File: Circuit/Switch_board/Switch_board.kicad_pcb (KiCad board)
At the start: 2 copper layers, 50.8 x 31.7 mm, 31 parts, among them J1 switch_mode, J2 switch, P1 XT30, Q1 2N7002, Q2 2N7002, Q3 2N7002, Q4 2N7002, U1 DRV5023

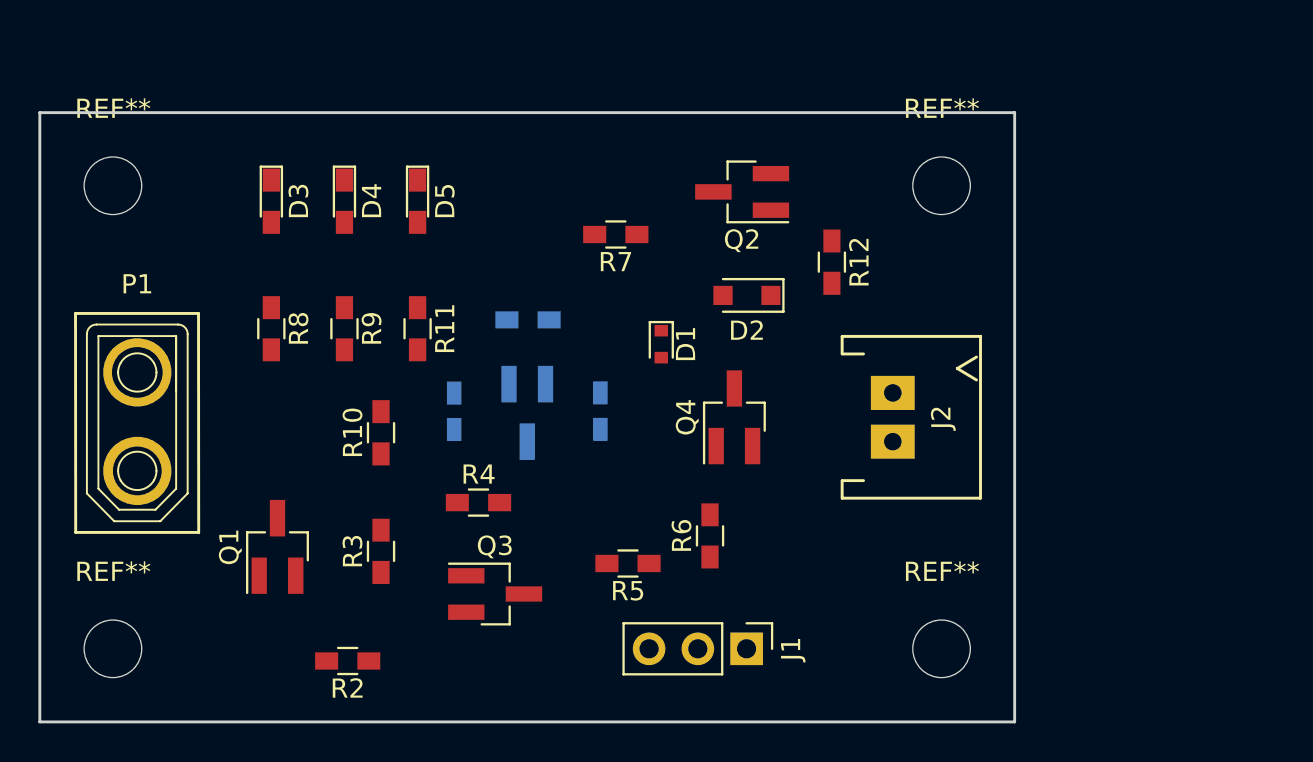
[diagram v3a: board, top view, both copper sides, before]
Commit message: added traces into pcb of Switch_board
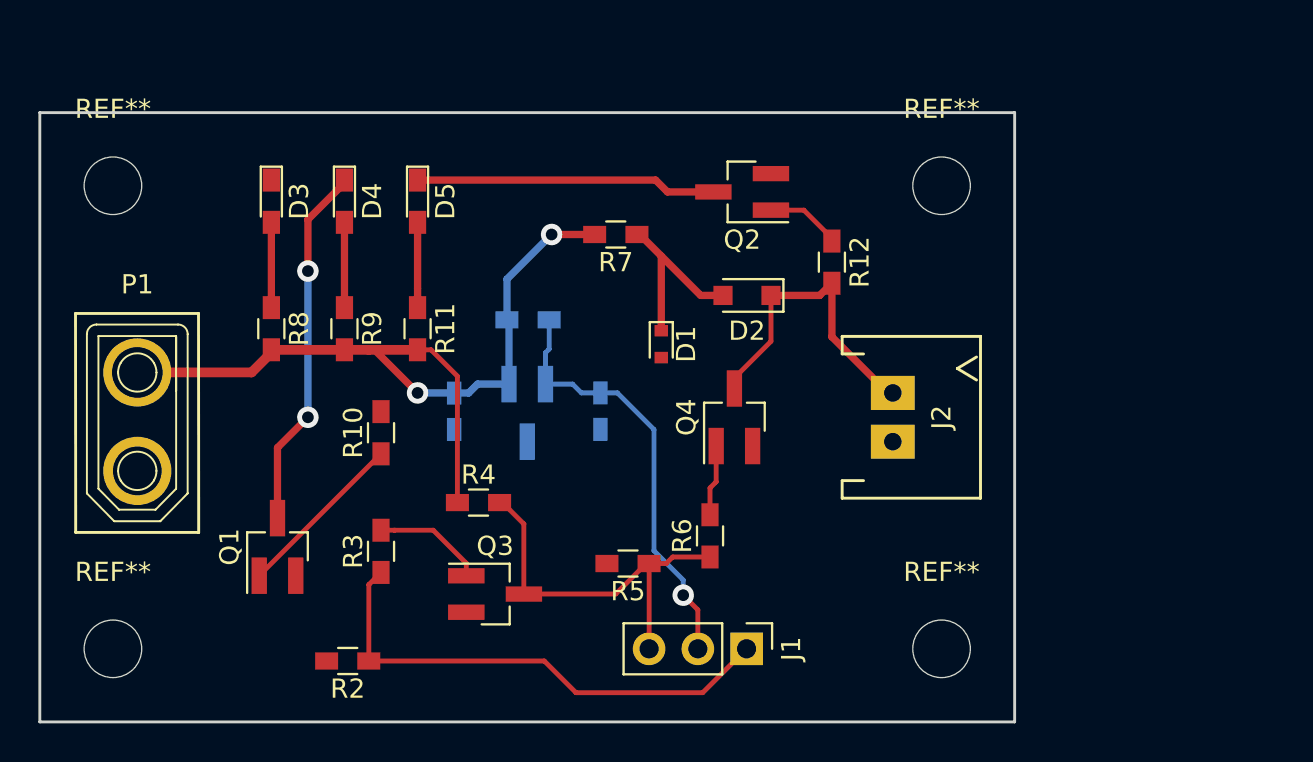
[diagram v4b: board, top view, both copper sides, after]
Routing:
- net VCC: track 0.00 -> 43.9 mm, vias 0 -> 2
- net Net-(J1-Pad1): track 0.00 -> 26.2 mm
- net hall_sensor_out: track 0.00 -> 22.4 mm, vias 0 -> 1
- net Net-(J1-Pad3): track 0.00 -> 20.3 mm
- net Net-(D4-Pad1): track 0.00 -> 19.1 mm, vias 0 -> 2
- net +switch: track 0.00 -> 16.3 mm
- net Net-(D5-Pad1): track 0.00 -> 15.7 mm
- net Net-(D1-Pad1): track 0.00 -> 9.70 mm
- net Net-(Q1-Pad1): track 0.00 -> 8.98 mm
- net Net-(Q3-Pad1): track 0.00 -> 5.81 mm
- net Net-(D5-Pad2): track 0.00 -> 4.44 mm
- net Net-(D4-Pad2): track 0.00 -> 4.44 mm
- net Net-(D3-Pad2): track 0.00 -> 4.44 mm
- net Net-(Q2-Pad1): track 0.00 -> 3.93 mm
- net Net-(Q4-Pad1): track 0.00 -> 3.71 mm
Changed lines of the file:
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@@
 (kicad_pcb (version 4) (host pcbnew 4.0.7)
   (general
-    (links 0)
+    (links 44)
     (no_connects 44)
-    (area 135.168857 102.398142 190.979 141.493286)
+    (area 136.041714 103.668142 194.158286 141.019)
     (thickness 1.6)
     (drawings 4)
-    (tracks 0)
+    (tracks 93)
     (zones 0)
     (modules 31)
@@
   (setup
     (last_trace_width 0.254)
+    (user_trace_width 0.381)
+    (user_trace_width 0.508)
     (trace_clearance 0.254)
     (zone_clearance 0.508)
@@
   (gr_line (start 190.5 139.7) (end 190.5 107.95) (layer Edge.Cuts) (width 0.15))
   (gr_line (start 139.7 139.7) (end 190.5 139.7) (layer Edge.Cuts) (width 0.15))
+  (segment (start 161.46 128.27) (end 161.46 121.681) (width 0.254) (layer F.Cu) (net 1))
+  (segment (start 161.46 121.681) (end 160.089 120.31) (width 0.254) (layer F.Cu) (net 1))
+  (segment (start 160.089 120.31) (end 159.385 120.31) (width 0.254) (layer F.Cu) (net 1))
+  (segment (start 166.37 114.3) (end 168.615 114.3) (width 0.381) (layer F.Cu) (net 1))
+  (segment (start 164.043 118.745) (end 164.043 116.627) (width 0.381) (layer B.Cu) (net 1))
+  (segment (start 164.043 116.627) (end 166.37 114.3) (width 0.381) (layer B.Cu) (net 1))
+  (segment (start 164.15 122.095) (end 164.15 118.852) (width 0.381) (layer B.Cu) (net 1))
+  (segment (start 164.15 118.852) (end 164.043 118.745) (width 0.381) (layer B.Cu) (net 1))
+  (segment (start 162.046 122.56) (end 162.511 122.095) (width 0.381) (layer B.Cu) (net 1))
+  (segment (start 162.511 122.095) (end 164.15 122.095) (width 0.381) (layer B.Cu) (net 1))
+  (segment (start 161.29 122.56) (end 162.046 122.56) (width 0.381) (layer B.Cu) (net 1))
+  (segment (start 159.385 122.555) (end 161.285 122.555) (width 0.381) (layer B.Cu) (net 1))
+  (segment (start 161.285 122.555) (end 161.29 122.56) (width 0.381) (layer B.Cu) (net 1))
+  (segment (start 156.845 120.31) (end 157.14 120.31) (width 0.381) (layer F.Cu) (net 1))
+  (segment (start 157.14 120.31) (end 159.385 122.555) (width 0.381) (layer F.Cu) (net 1))
+  (segment (start 156.845 120.31) (end 159.385 120.31) (width 0.508) (layer F.Cu) (net 1))
+  (segment (start 155.575 120.31) (end 156.845 120.31) (width 0.508) (layer F.Cu) (net 1))
+  (via (at 166.37 114.3) (size 1.1176) (drill 0.6096) (layers F.Cu B.Cu) (net 1))
+  (via (at 159.385 122.555) (size 1.1176) (drill 0.6096) (layers F.Cu B.Cu) (net 1))
+  (segment (start 151.765 120.31) (end 155.575 120.31) (width 0.508) (layer F.Cu) (net 1))
+  (segment (start 144.78 121.4882) (end 150.7368 121.4882) (width 0.508) (layer F.Cu) (net 1))
+  (segment (start 150.7368 121.4882) (end 151.765 120.46) (width 0.508) (layer F.Cu) (net 1))
+  (segment (start 151.765 120.46) (end 151.765 120.31) (width 0.508) (layer F.Cu) (net 1))
+  (segment (start 172.085 115.42) (end 174.14 117.475) (width 0.381) (layer F.Cu) (net 3))
+  (segment (start 174.14 117.475) (end 175.3 117.475) (width 0.381) (layer F.Cu) (net 3))
+  (segment (start 172.085 115.42) (end 172.085 119.315) (width 0.381) (layer F.Cu) (net 3))
+  (segment (start 170.815 114.3) (end 170.965 114.3) (width 0.381) (layer F.Cu) (net 3))
+  (segment (start 170.965 114.3) (end 172.085 115.42) (width 0.381) (layer F.Cu) (net 3))
+  (segment (start 174.244 138.176) (end 176.53 135.89) (width 0.254) (layer F.Cu) (net 4))
+  (segment (start 167.64 138.176) (end 174.244 138.176) (width 0.254) (layer F.Cu) (net 4))
+  (segment (start 165.989 136.525) (end 167.64 138.176) (width 0.254) (layer F.Cu) (net 4))
+  (segment (start 156.845 136.525) (end 165.989 136.525) (width 0.254) (layer F.Cu) (net 4))
+  (segment (start 156.845 136.525) (end 156.845 132.545) (width 0.254) (layer F.Cu) (net 4))
+  (segment (start 156.845 132.545) (end 157.48 131.91) (width 0.254) (layer F.Cu) (net 4))
+  (segment (start 171.45 131.445) (end 171.45 135.89) (width 0.254) (layer F.Cu) (net 5))
+  (segment (start 172.339 131.445) (end 172.679 131.105) (width 0.254) (layer F.Cu) (net 5))
+  (segment (start 172.679 131.105) (end 174.625 131.105) (width 0.254) (layer F.Cu) (net 5))
+  (segment (start 171.45 131.445) (end 172.339 131.445) (width 0.254) (layer F.Cu) (net 5))
+  (segment (start 164.925 133.035) (end 169.71 133.035) (width 0.254) (layer F.Cu) (net 5))
+  (segment (start 169.71 133.035) (end 171.3 131.445) (width 0.254) (layer F.Cu) (net 5))
+  (segment (start 171.3 131.445) (end 171.45 131.445) (width 0.254) (layer F.Cu) (net 5))
+  (segment (start 163.66 128.27) (end 163.81 128.27) (width 0.254) (layer F.Cu) (net 5))
+  (segment (start 163.81 128.27) (end 164.925 129.385) (width 0.254) (layer F.Cu) (net 5))
+  (segment (start 164.925 129.385) (end 164.925 133.035) (width 0.254) (layer F.Cu) (net 5))
+  (segment (start 151.135 132.08) (end 151.135 132.075) (width 0.254) (layer F.Cu) (net 6))
+  (segment (start 151.135 132.075) (end 157.48 125.73) (width 0.254) (layer F.Cu) (net 6))
+  (segment (start 177.8 113.03) (end 179.515 113.03) (width 0.254) (layer F.Cu) (net 7))
+  (segment (start 179.515 113.03) (end 180.975 114.49) (width 0.254) (layer F.Cu) (net 7))
+  (segment (start 180.975 114.49) (end 180.975 114.64) (width 0.254) (layer F.Cu) (net 7))
+  (segment (start 166.05 120.462) (end 166.243 120.269) (width 0.254) (layer B.Cu) (net 8))
+  (segment (start 166.243 120.269) (end 166.243 118.745) (width 0.254) (layer B.Cu) (net 8))
+  (segment (start 166.05 122.095) (end 166.05 120.462) (width 0.254) (layer B.Cu) (net 8))
+  (segment (start 167.465 122.095) (end 167.925 122.555) (width 0.254) (layer B.Cu) (net 8))
+  (segment (start 167.925 122.555) (end 168.91 122.555) (width 0.254) (layer B.Cu) (net 8))
+  (segment (start 166.05 122.095) (end 167.465 122.095) (width 0.254) (layer B.Cu) (net 8))
+  (segment (start 173.228 133.096) (end 173.228 132.305738) (width 0.254) (layer B.Cu) (net 8))
+  (segment (start 173.228 132.305738) (end 171.704 130.781738) (width 0.254) (layer B.Cu) (net 8))
+  (segment (start 171.704 130.781738) (end 171.704 124.46) (width 0.254) (layer B.Cu) (net 8))
+  (segment (start 171.704 124.46) (end 169.799 122.555) (width 0.254) (layer B.Cu) (net 8))
+  (segment (start 169.799 122.555) (end 168.91 122.555) (width 0.254) (layer B.Cu) (net 8))
+  (segment (start 173.99 135.89) (end 173.99 133.858) (width 0.254) (layer F.Cu) (net 8))
+  (segment (start 173.99 133.858) (end 173.228 133.096) (width 0.254) (layer F.Cu) (net 8))
+  (via (at 173.228 133.096) (size 1.1176) (drill 0.6096) (layers F.Cu B.Cu) (net 8))
+  (segment (start 175.895 122.325) (end 175.895 121.775) (width 0.254) (layer F.Cu) (net 9))
+  (segment (start 175.895 121.775) (end 177.8 119.87) (width 0.254) (layer F.Cu) (net 9))
+  (segment (start 177.8 119.87) (end 177.8 117.475) (width 0.254) (layer F.Cu) (net 9))
+  (segment (start 180.975 116.84) (end 180.975 119.634) (width 0.381) (layer F.Cu) (net 9))
+  (segment (start 180.975 119.634) (end 183.896 122.555) (width 0.381) (layer F.Cu) (net 9))
+  (segment (start 183.896 122.555) (end 184.15 122.555) (width 0.381) (layer F.Cu) (net 9))
+  (segment (start 177.8 117.475) (end 180.34 117.475) (width 0.381) (layer F.Cu) (net 9))
+  (segment (start 180.34 117.475) (end 180.975 116.84) (width 0.381) (layer F.Cu) (net 9))
+  (segment (start 151.765 118.11) (end 151.765 113.665) (width 0.381) (layer F.Cu) (net 10))
+  (segment (start 153.67 123.825) (end 152.085 125.41) (width 0.381) (layer F.Cu) (net 11))
+  (segment (start 152.085 125.41) (end 152.085 129.08) (width 0.381) (layer F.Cu) (net 11))
+  (segment (start 153.67 116.205) (end 153.67 123.825) (width 0.381) (layer B.Cu) (net 11))
+  (via (at 153.67 123.825) (size 1.1176) (drill 0.6096) (layers F.Cu B.Cu) (net 11))
+  (segment (start 155.575 111.465) (end 155.575 111.615) (width 0.381) (layer F.Cu) (net 11))
+  (segment (start 155.575 111.615) (end 153.67 113.52) (width 0.381) (layer F.Cu) (net 11))
+  (segment (start 153.67 113.52) (end 153.67 116.205) (width 0.381) (layer F.Cu) (net 11))
+  (via (at 153.67 116.205) (size 1.1176) (drill 0.6096) (layers F.Cu B.Cu) (net 11))
+  (segment (start 155.575 118.11) (end 155.575 113.665) (width 0.381) (layer F.Cu) (net 12))
+  (segment (start 171.79 111.465) (end 172.405 112.08) (width 0.381) (layer F.Cu) (net 13))
+  (segment (start 172.405 112.08) (end 174.8 112.08) (width 0.381) (layer F.Cu) (net 13))
+  (segment (start 159.385 111.465) (end 171.79 111.465) (width 0.381) (layer F.Cu) (net 13))
+  (segment (start 159.385 118.11) (end 159.385 117.129) (width 0.381) (layer F.Cu) (net 14))
+  (segment (start 159.385 117.129) (end 159.385 113.665) (width 0.381) (layer F.Cu) (net 14))
+  (segment (start 161.925 132.085) (end 161.925 131.431) (width 0.254) (layer F.Cu) (net 15))
+  (segment (start 161.925 131.431) (end 160.204 129.71) (width 0.254) (layer F.Cu) (net 15))
+  (segment (start 160.204 129.71) (end 158.184 129.71) (width 0.254) (layer F.Cu) (net 15))
+  (segment (start 158.184 129.71) (end 157.48 129.71) (width 0.254) (layer F.Cu) (net 15))
+  (segment (start 174.625 127.508) (end 174.945 127.188) (width 0.254) (layer F.Cu) (net 16))
+  (segment (start 174.945 127.188) (end 174.945 125.325) (width 0.254) (layer F.Cu) (net 16))
+  (segment (start 174.625 128.905) (end 174.625 127.508) (width 0.254) (layer F.Cu) (net 16))
 )

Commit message: filled GND zone for Switch_board
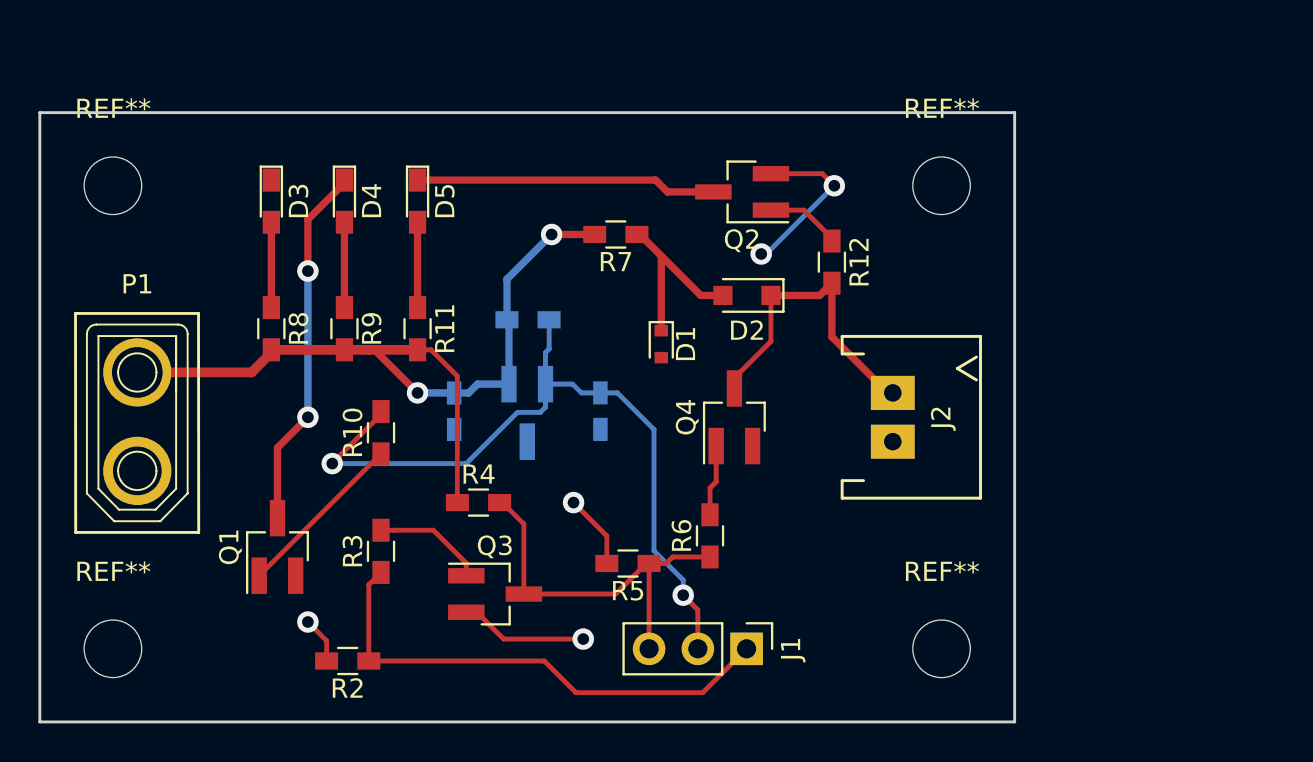
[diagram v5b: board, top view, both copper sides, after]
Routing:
- net GND: track 0.00 -> 21.9 mm, vias 0 -> 5
- net hall_sensor_out: track 22.4 -> 39.7 mm, vias 1 -> 2
- added copper zone on B.Cu, net GND
- added copper zone on F.Cu, net GND
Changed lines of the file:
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@@
   (general
     (links 44)
-    (no_connects 44)
+    (no_connects 0)
     (area 136.041714 103.668142 194.158286 141.019)
     (thickness 1.6)
     (drawings 4)
-    (tracks 93)
+    (tracks 118)
     (zones 0)
     (modules 31)
@@
     (pad_to_mask_clearance 0.2)
     (aux_axis_origin 0 0)
-    (visible_elements FFFFFF7F)
+    (visible_elements FFFFEF7F)
     (pcbplotparams
       (layerselection 0x00030_80000001)
@@
   (segment (start 150.7368 121.4882) (end 151.765 120.46) (width 0.508) (layer F.Cu) (net 1))
   (segment (start 151.765 120.46) (end 151.765 120.31) (width 0.508) (layer F.Cu) (net 1))
+  (segment (start 163.872 135.382) (end 168.021 135.382) (width 0.254) (layer F.Cu) (net 2))
+  (segment (start 161.925 133.985) (end 162.475 133.985) (width 0.254) (layer F.Cu) (net 2))
+  (segment (start 162.475 133.985) (end 163.872 135.382) (width 0.254) (layer F.Cu) (net 2))
+  (segment (start 154.645 136.525) (end 154.645 135.468) (width 0.254) (layer F.Cu) (net 2))
+  (segment (start 154.645 135.468) (end 153.67 134.493) (width 0.254) (layer F.Cu) (net 2))
+  (via (at 153.67 134.493) (size 1.1176) (drill 0.6096) (layers F.Cu B.Cu) (net 2))
+  (via (at 168.021 135.382) (size 1.1176) (drill 0.6096) (layers F.Cu B.Cu) (net 2))
+  (segment (start 181.102 111.76) (end 177.546 115.316) (width 0.254) (layer B.Cu) (net 2))
+  (segment (start 177.546 115.316) (end 177.292 115.316) (width 0.254) (layer B.Cu) (net 2))
+  (via (at 177.292 115.316) (size 1.1176) (drill 0.6096) (layers F.Cu B.Cu) (net 2))
+  (segment (start 177.8 111.13) (end 180.472 111.13) (width 0.254) (layer F.Cu) (net 2))
+  (segment (start 180.472 111.13) (end 181.102 111.76) (width 0.254) (layer F.Cu) (net 2))
+  (via (at 181.102 111.76) (size 1.1176) (drill 0.6096) (layers F.Cu B.Cu) (net 2))
+  (segment (start 169.25 131.445) (end 169.25 130.007) (width 0.254) (layer F.Cu) (net 2))
+  (segment (start 169.25 130.007) (end 167.513 128.27) (width 0.254) (layer F.Cu) (net 2))
+  (via (at 167.513 128.27) (size 1.1176) (drill 0.6096) (layers F.Cu B.Cu) (net 2))
   (segment (start 172.085 115.42) (end 174.14 117.475) (width 0.381) (layer F.Cu) (net 3))
   (segment (start 174.14 117.475) (end 175.3 117.475) (width 0.381) (layer F.Cu) (net 3))
@@
   (segment (start 179.515 113.03) (end 180.975 114.49) (width 0.254) (layer F.Cu) (net 7))
   (segment (start 180.975 114.49) (end 180.975 114.64) (width 0.254) (layer F.Cu) (net 7))
+  (segment (start 154.94 126.238) (end 161.925 126.238) (width 0.254) (layer B.Cu) (net 8))
+  (segment (start 161.925 126.238) (end 164.592 123.571) (width 0.254) (layer B.Cu) (net 8))
+  (segment (start 164.592 123.571) (end 165.778 123.571) (width 0.254) (layer B.Cu) (net 8))
+  (segment (start 165.778 123.571) (end 166.05 123.299) (width 0.254) (layer B.Cu) (net 8))
+  (segment (start 166.05 123.299) (end 166.05 122.095) (width 0.254) (layer B.Cu) (net 8))
+  (segment (start 157.48 123.53) (end 157.48 123.68) (width 0.254) (layer F.Cu) (net 8))
+  (segment (start 157.48 123.68) (end 154.94 126.22) (width 0.254) (layer F.Cu) (net 8))
+  (segment (start 154.94 126.22) (end 154.94 126.238) (width 0.254) (layer F.Cu) (net 8))
+  (via (at 154.94 126.238) (size 1.1176) (drill 0.6096) (layers F.Cu B.Cu) (net 8))
   (segment (start 166.05 120.462) (end 166.243 120.269) (width 0.254) (layer B.Cu) (net 8))
   (segment (start 166.243 120.269) (end 166.243 118.745) (width 0.254) (layer B.Cu) (net 8))
@@
   (segment (start 174.945 127.188) (end 174.945 125.325) (width 0.254) (layer F.Cu) (net 16))
   (segment (start 174.625 128.905) (end 174.625 127.508) (width 0.254) (layer F.Cu) (net 16))
+  (zone (net 2) (net_name GND) (layer F.Cu) (hatch edge 0.508)
+    (connect_pads yes (clearance 0.508))
+    (min_thickness 0.254)
+    (fill yes (arc_segments 16) (thermal_gap 0.508) (thermal_bridge_width 0.508))
+    (polygon
+      (pts
+        (xy 139.7 107.95) (xy 190.5 107.95) (xy 190.5 139.7) (xy 139.7 139.7)
+      )
+    )
+  )
+  (zone (net 2) (net_name GND) (layer B.Cu) (hatch edge 0.508)
+    (connect_pads yes (clearance 0.508))
+    (min_thickness 0.254)
+    (fill yes (arc_segments 16) (thermal_gap 0.508) (thermal_bridge_width 0.508))
+    (polygon
+      (pts
+        (xy 190.5 139.7) (xy 190.5 107.95) (xy 139.7 107.95) (xy 139.7 139.7)
+      )
+    )
+  )
 )
